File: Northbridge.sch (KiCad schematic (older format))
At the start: 21 parts, among them J3 JTAG

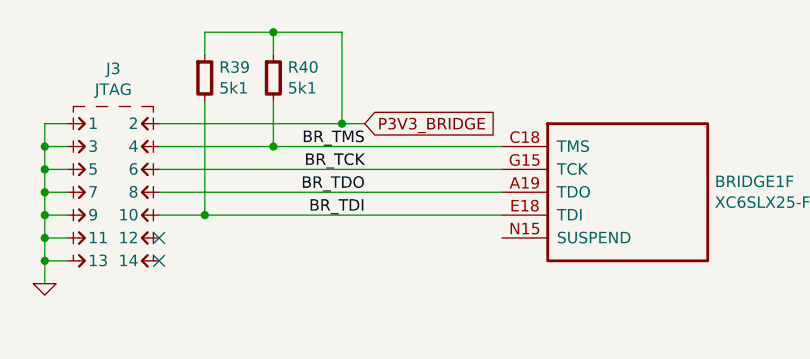
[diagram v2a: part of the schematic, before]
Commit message: Route FPGA suspend signals
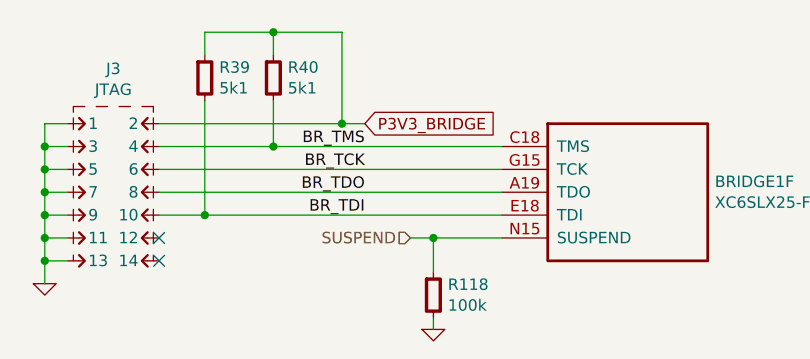
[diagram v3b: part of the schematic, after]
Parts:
- added R118: 100k, IPC7351-Nominal:RESC1005X40, symbol R-0402
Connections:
- net GND: now also R118.2
- net SUSPEND: now reaches BRIDGE1.N15 (SUSPEND)
- net SUSPEND: now also R118.1
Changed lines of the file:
@@
 P 5900 14700
 AR Path="/5763AB3B/5799D8FC" Ref="#PWR?"  Part="1"
-AR Path="/5763A638/5799D8FC" Ref="#PWR157"  Part="1"
-F 0 "#PWR157" H 5900 14700 30  0001 C CNN
+AR Path="/5763A638/5799D8FC" Ref="#PWR158"  Part="1"
+F 0 "#PWR158" H 5900 14700 30  0001 C CNN
 F 1 "GND" H 5900 14630 30  0001 C CNN
 F 2 "" H 5900 14700 60  0000 C CNN
@@
 P3V3_BRIDGE
 $Comp
-L GND #PWR156
+L GND #PWR157
 U 1 1 5799E8A3
 P 5600 12850
-F 0 "#PWR156" H 5600 12850 30  0001 C CNN
+F 0 "#PWR157" H 5600 12850 30  0001 C CNN
 F 1 "GND" H 5600 12780 30  0001 C CNN
 F 2 "" H 5600 12850 60  0000 C CNN
@@
 P 7200 14800
 AR Path="/5763AB3B/57A7C581" Ref="#PWR?"  Part="1"
-AR Path="/5763A638/57A7C581" Ref="#PWR158"  Part="1"
-F 0 "#PWR158" H 7200 14800 30  0001 C CNN
+AR Path="/5763A638/57A7C581" Ref="#PWR159"  Part="1"
+F 0 "#PWR159" H 7200 14800 30  0001 C CNN
 F 1 "GND" H 7200 14730 30  0001 C CNN
 F 2 "" H 7200 14800 60  0000 C CNN
@@
 	1    0    0    -1
 $EndComp
+Text Notes 4400 1900 0    100  ~ 0
+3.3V BANK
+Text Notes 4400 2300 0    60   ~ 0
+- PCI\n- LIMB\n- Configuration
+Text Notes 8600 1900 0    100  ~ 0
+1.5V BANKS
+Text Notes 8600 2200 0    60   ~ 0
+- SDRAM\n- CPU
+Text HLabel 8800 14600 0    50   Input ~ 0
+SUSPEND
 Wire Wire Line
 	17900 9000 18500 9000
@@
 Wire Wire Line
 	18000 8900 18500 8900
-Text Notes 4400 1900 0    100  ~ 0
-3.3V BANK
-Text Notes 4400 2300 0    60   ~ 0
-- PCI\n- LIMB\n- Configuration
-Text Notes 8600 1900 0    100  ~ 0
-1.5V BANKS
-Text Notes 8600 2200 0    60   ~ 0
-- SDRAM\n- CPU
 Wire Notes Line
 	8500 1900 8500 1700
@@
 Wire Notes Line
 	15600 1700 15600 2000
+Wire Wire Line
+	9200 14600 8800 14600
+$Comp
+L R-0402 R?
+U 1 1 57A6F986
+P 8900 14850
+AR Path="/5763AB3B/57A6F986" Ref="R?"  Part="1"
+AR Path="/5763A638/57A6F986" Ref="R118"  Part="1"
+F 0 "R118" H 8963 14896 50  0000 L CNN
+F 1 "100k" H 8963 14805 50  0000 L CNN
+F 2 "IPC7351-Nominal:RESC1005X40" H 8900 14850 50  0001 C CNN
+F 3 "" H 8900 14900 60  0000 C CNN
+F 4 "RES SMD 100k 1% [0402]" H 9650 15400 60  0001 C CNN "BOM"
+	1    8900 14850
+	1    0    0    -1
+$EndComp
+Wire Wire Line
+	8900 14750 8900 14600
+Connection ~ 8900 14600
+$Comp
+L GND #PWR160
+U 1 1 57A6FC44
+P 8900 15000
+F 0 "#PWR160" H 8900 15000 30  0001 C CNN
+F 1 "GND" H 8900 14930 30  0001 C CNN
+F 2 "" H 8900 15000 60  0000 C CNN
+F 3 "" H 8900 15000 60  0000 C CNN
+	1    8900 15000
+	1    0    0    -1
+$EndComp
+Wire Wire Line
+	8900 15000 8900 14950
 $EndSCHEMATC

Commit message: Fix footprint errors and adjust DE-9 footprint
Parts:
- SODIMM1: footprint (none) -> conn-te:SODIMM-2013289
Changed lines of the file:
@@
 F 0 "SODIMM1" H 19100 3267 50  0000 C CNN
 F 1 "DDR3-SODIMM" H 19100 3176 50  0000 C CNN
-F 2 "" H 19000 4000 50  0001 C CNN
+F 2 "conn-te:SODIMM-2013289" H 19000 4000 50  0001 C CNN
 F 3 "" H 19100 4100 50  0001 C CNN
 F 4 "DIST DIGIKEY A116236CT-ND" H 19100 3000 60  0001 C CNN "BOM"

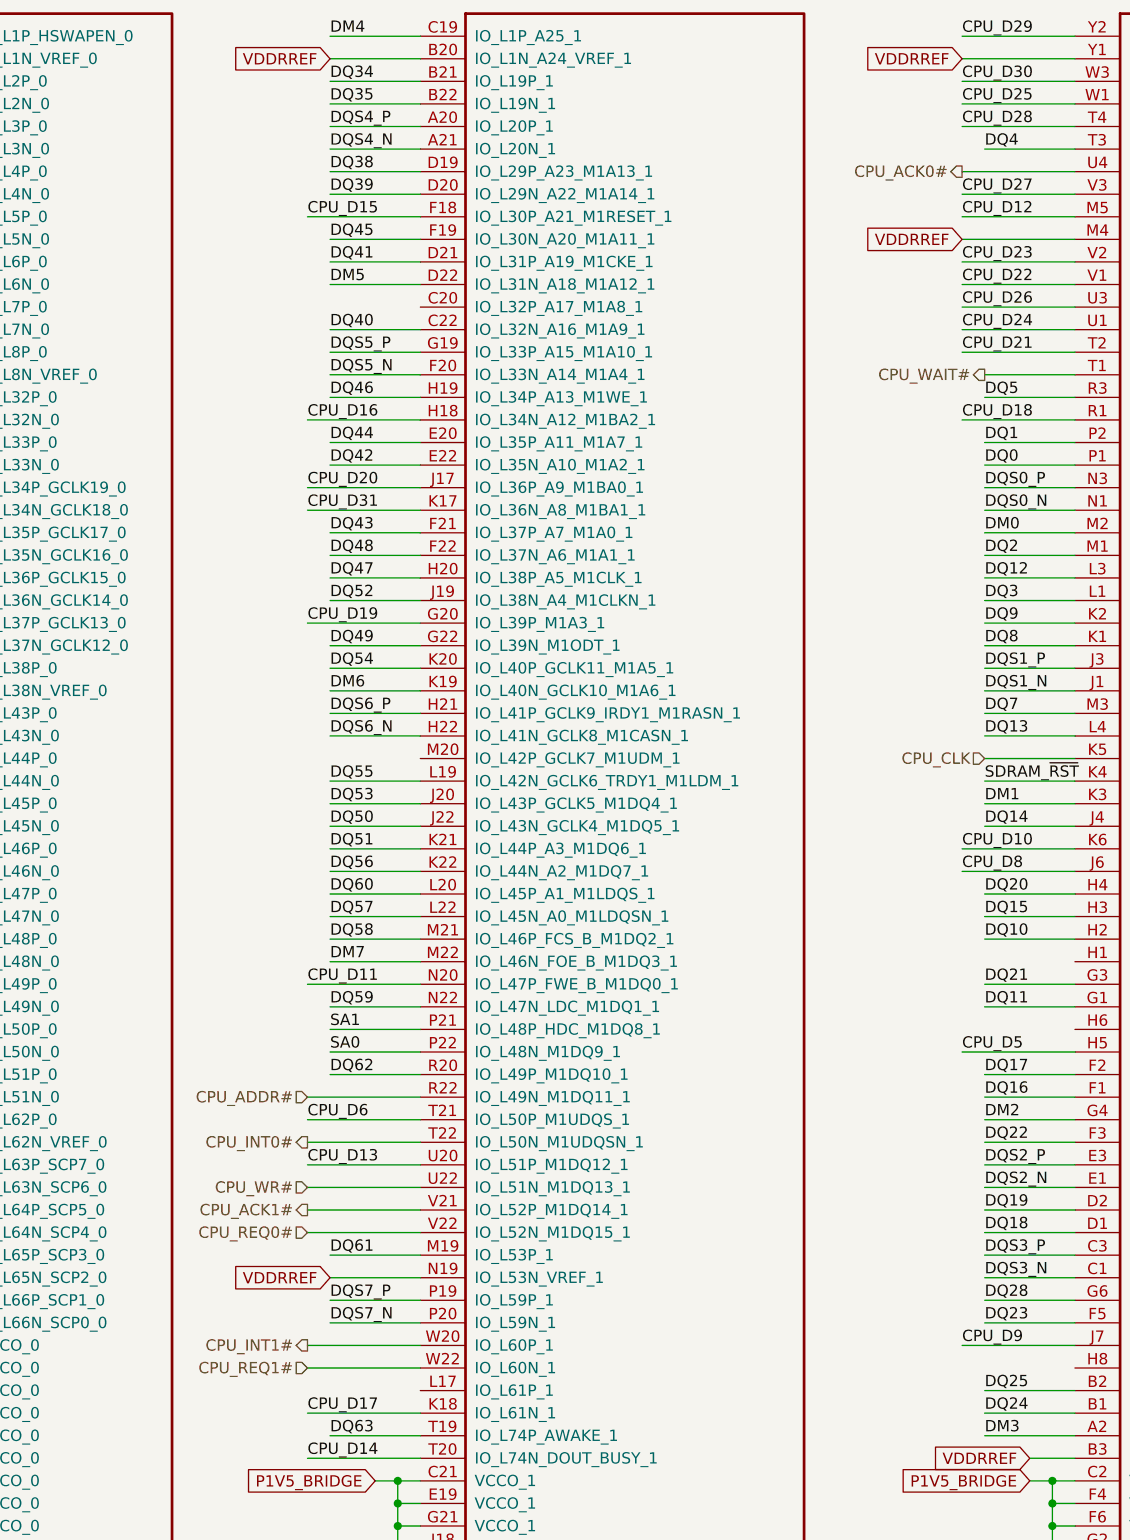
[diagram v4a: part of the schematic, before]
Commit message: Rename active-low signals for consistency
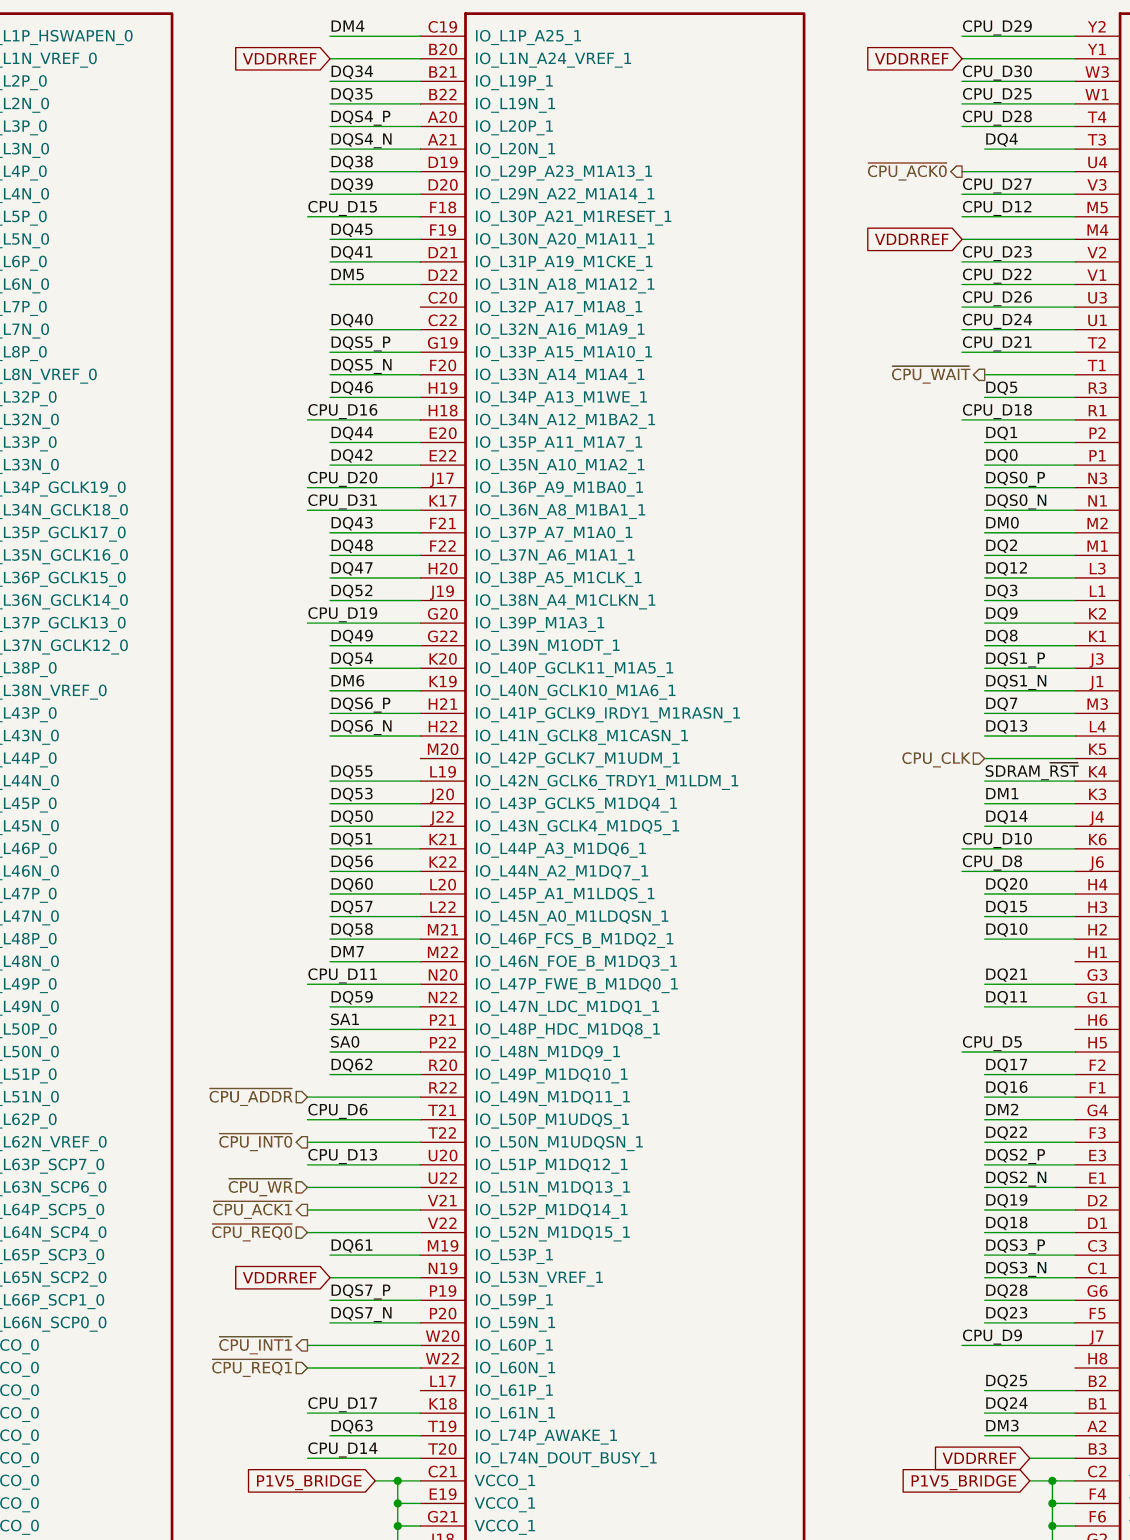
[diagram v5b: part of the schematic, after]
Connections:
- net CPU_ACK0# renamed ~CPU_ACK0
- net CPU_ACK1# renamed ~CPU_ACK1
- net CPU_ADDR# renamed ~CPU_ADDR
- net CPU_INT0# renamed ~CPU_INT0
- net CPU_INT1# renamed ~CPU_INT1
- net CPU_REQ0# renamed ~CPU_REQ0
- net CPU_REQ1# renamed ~CPU_REQ1
- net CPU_WAIT# renamed ~CPU_WAIT
- net CPU_WR# renamed ~CPU_WR
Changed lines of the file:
@@
 CPU_D[0..31]
 Text HLabel 13200 4300 0    50   Output ~ 0
-CPU_WAIT#
+~CPU_WAIT
 Text HLabel 10200 7500 0    50   Input ~ 0
-CPU_ADDR#
+~CPU_ADDR
 Text HLabel 10200 7900 0    50   Input ~ 0
-CPU_WR#
+~CPU_WR
 Text HLabel 13200 6000 0    50   Input ~ 0
 CPU_CLK
 Text HLabel 10200 8100 0    50   Input ~ 0
-CPU_REQ0#
+~CPU_REQ0
 Text HLabel 13100 3400 0    50   Output ~ 0
-CPU_ACK0#
+~CPU_ACK0
 Text HLabel 10200 8700 0    50   Input ~ 0
-CPU_REQ1#
+~CPU_REQ1
 Text HLabel 10200 8000 0    50   Output ~ 0
-CPU_ACK1#
+~CPU_ACK1
 Text HLabel 10200 7700 0    50   Output ~ 0
-CPU_INT0#
+~CPU_INT0
 Text HLabel 10200 8600 0    50   Output ~ 0
-CPU_INT1#
+~CPU_INT1
 Text HLabel 1700 13800 0    50   BiDi ~ 0
 PCI_AD[0..31]

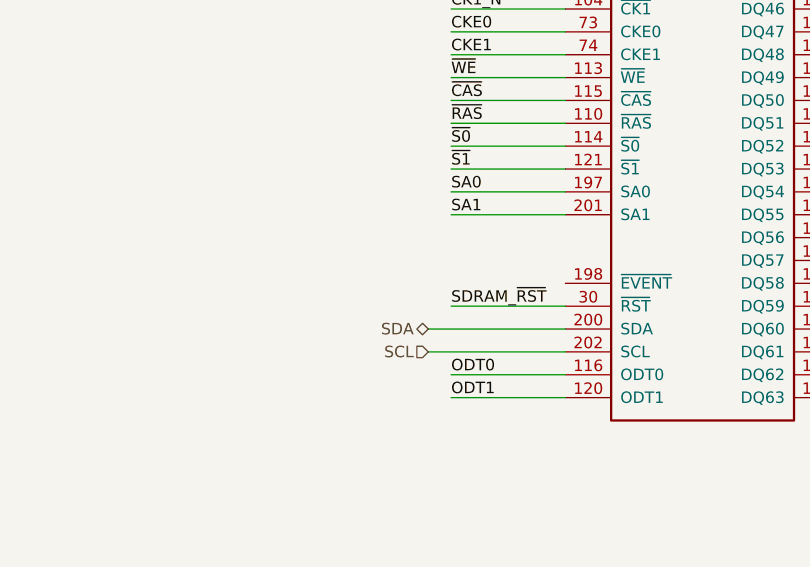
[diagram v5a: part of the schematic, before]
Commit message: Connect SDRAM EVENT# line
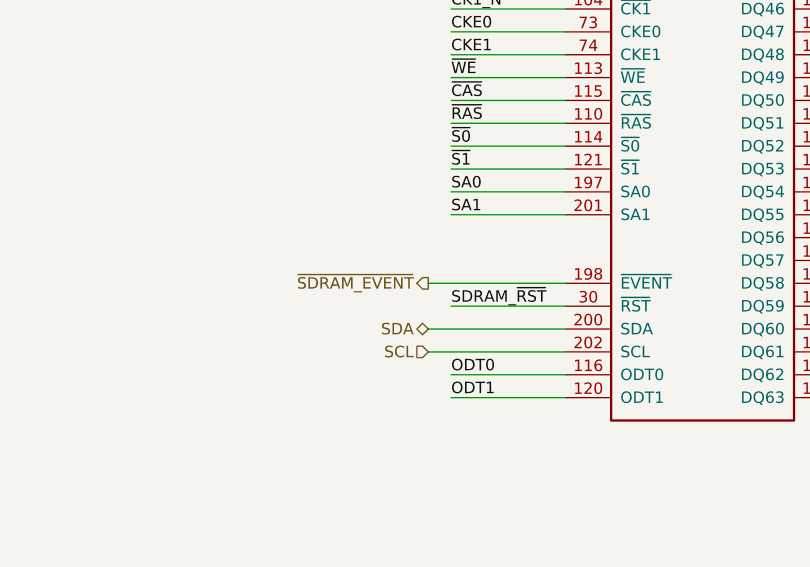
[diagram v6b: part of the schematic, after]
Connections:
- net ~SDRAM_EVENT: now reaches SODIMM1.198 (~EVENT)
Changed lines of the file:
@@
 $Descr C 22000 17000
 encoding utf-8
-Sheet 7 10
+Sheet 10 10
 Title "Northbridge"
 Date "2016-08-05"
@@
 Wire Wire Line
 	8900 15000 8900 14950
+Wire Wire Line
+	18500 8800 17900 8800
+Text HLabel 17900 8800 0    50   Output ~ 0
+~SDRAM_EVENT
 $EndSCHEMATC
